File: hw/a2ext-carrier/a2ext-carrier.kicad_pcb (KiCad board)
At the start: 2 copper layers, 99.7 x 78.7 mm, 14 parts, among them J1 Apple II slot, counter-clockw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, J2 Daughterboard IDC20, M1 WeAct RP2350B V1.0 (prepared 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

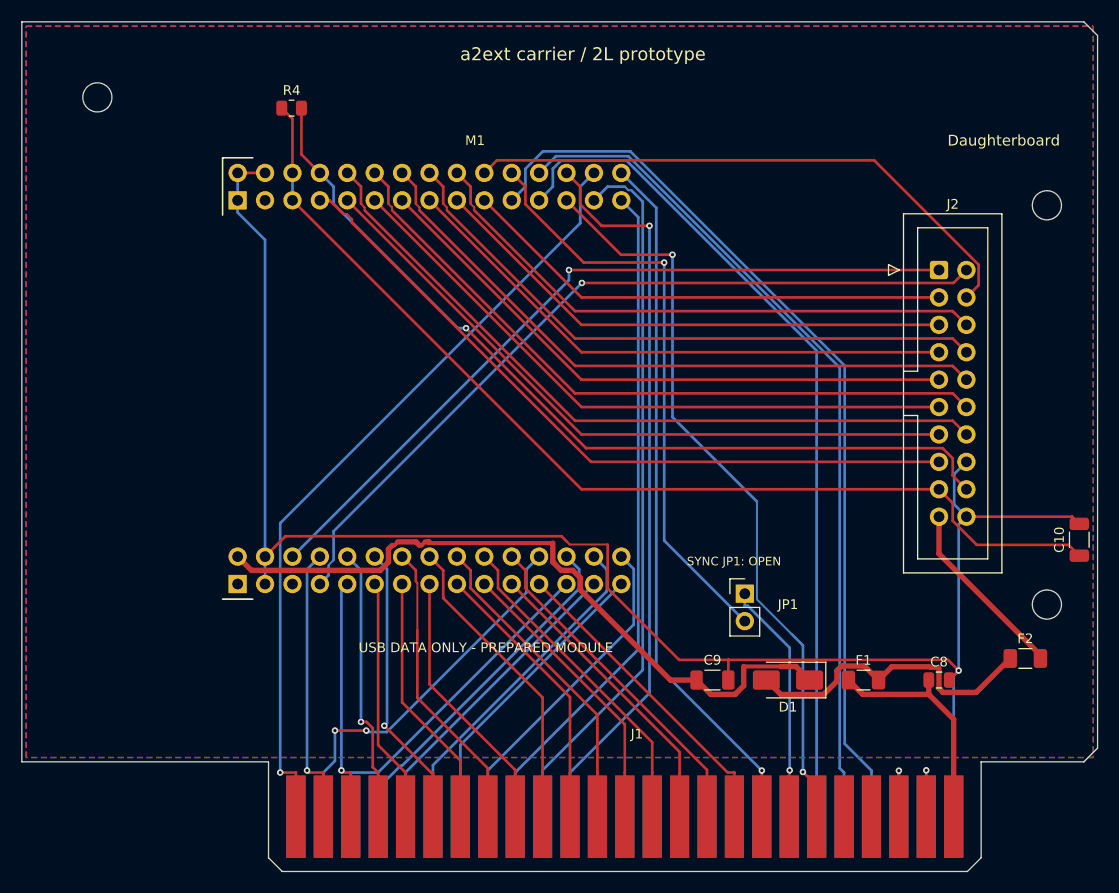
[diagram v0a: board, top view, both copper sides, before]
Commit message: Revise all prototype PCBs for through-hole assembly
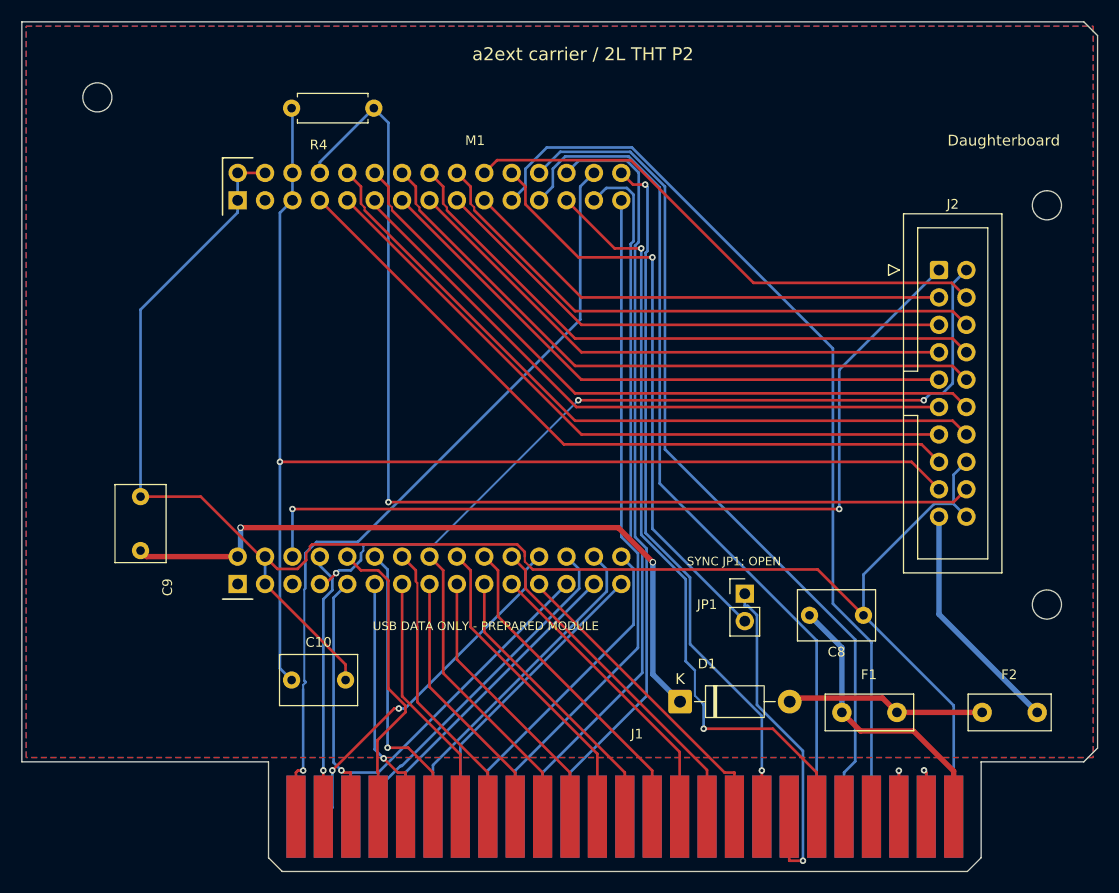
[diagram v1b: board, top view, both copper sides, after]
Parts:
- C10, C9: footprint A2Ext:C1206 -> A2Ext:C_Radial_5
- C8: footprint A2Ext:C0805 -> A2Ext:C_Radial_5
- D1: value SS14 -> 1N5819; footprint A2Ext:SS14 -> A2Ext:Schottky_DO41
- F1: footprint A2Ext:PTC1206 -> A2Ext:PTC_MF_R050
- F2: footprint A2Ext:PTC1206 -> A2Ext:PTC_MF_R010
- R4: footprint A2Ext:R0805 -> A2Ext:R_Axial_7.62
- moved C10 74.1 mm to (75.0, 111.0), turned to 0 degrees
- moved C9 54.3 mm to (61.0, 99.0), turned to 90 degrees
- moved C8 13.4 mm to (123.0, 105.0)
- moved D1 10.2 mm to (111.0, 113.0), turned to 0 degrees
- moved F2 6.40 mm to (139.0, 114.0)
- moved F1 3.61 mm to (126.0, 114.0)
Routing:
- net /+3V3: track 96.5 -> 116.1 mm, vias 0 -> 1
- net /RUN_N: track 80.6 -> 99.2 mm
- net /+5V_FUSED: track 29.3 -> 18.5 mm
- net /SLOT19_OPTIONAL: track 22.6 -> 32.5 mm
- net /UART_TX: track 71.5 -> 81.1 mm, vias 1 -> 2
- net /GND: track 162.4 -> 168.3 mm, vias 1 -> 0
- net /+5V_SLOT: track 21.6 -> 27.1 mm
- net /+5V_DB: track 17.0 -> 21.9 mm
- net /UART_RX: track 74.1 -> 78.1 mm, vias 1 -> 3
- net /IDC04_GPIO36: track 53.8 -> 50.4 mm
- net /A2: track 25.6 -> 28.4 mm, vias 1 -> 0
- net /D0: track 35.4 -> 33.0 mm
- net /IOSTRB_N: track 69.5 -> 71.9 mm
- net /PHI0: track 68.5 -> 70.8 mm, vias 1 -> 0
- net /IRQ_N: track 78.4 -> 79.9 mm
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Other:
- board text added: "a2ext carrier / 2L THT P2"
- board text removed: "a2ext carrier / 2L prototype"
